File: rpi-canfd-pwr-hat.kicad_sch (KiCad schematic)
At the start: 34 parts, among them J1 Raspberry_Pi, J5 Conn_01x04_Pin, U1 CAT24C256, U2 LM73100, U5 TPS56637

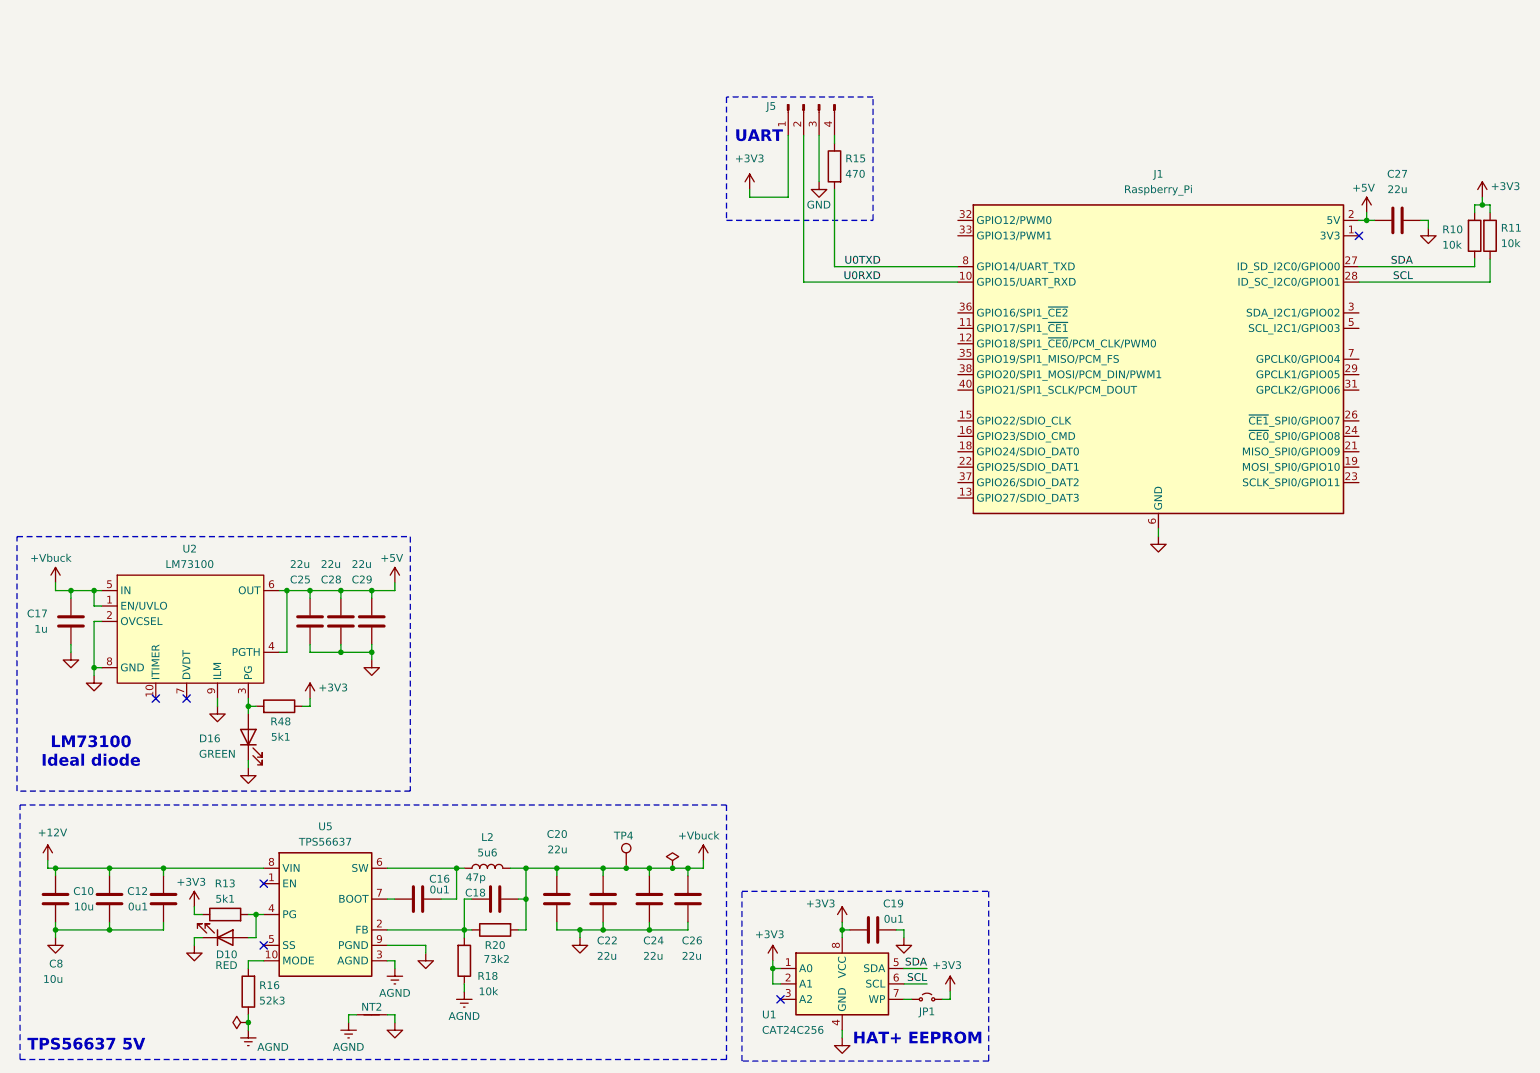
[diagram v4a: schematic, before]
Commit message: schem: add TPS259472A 5A efuse
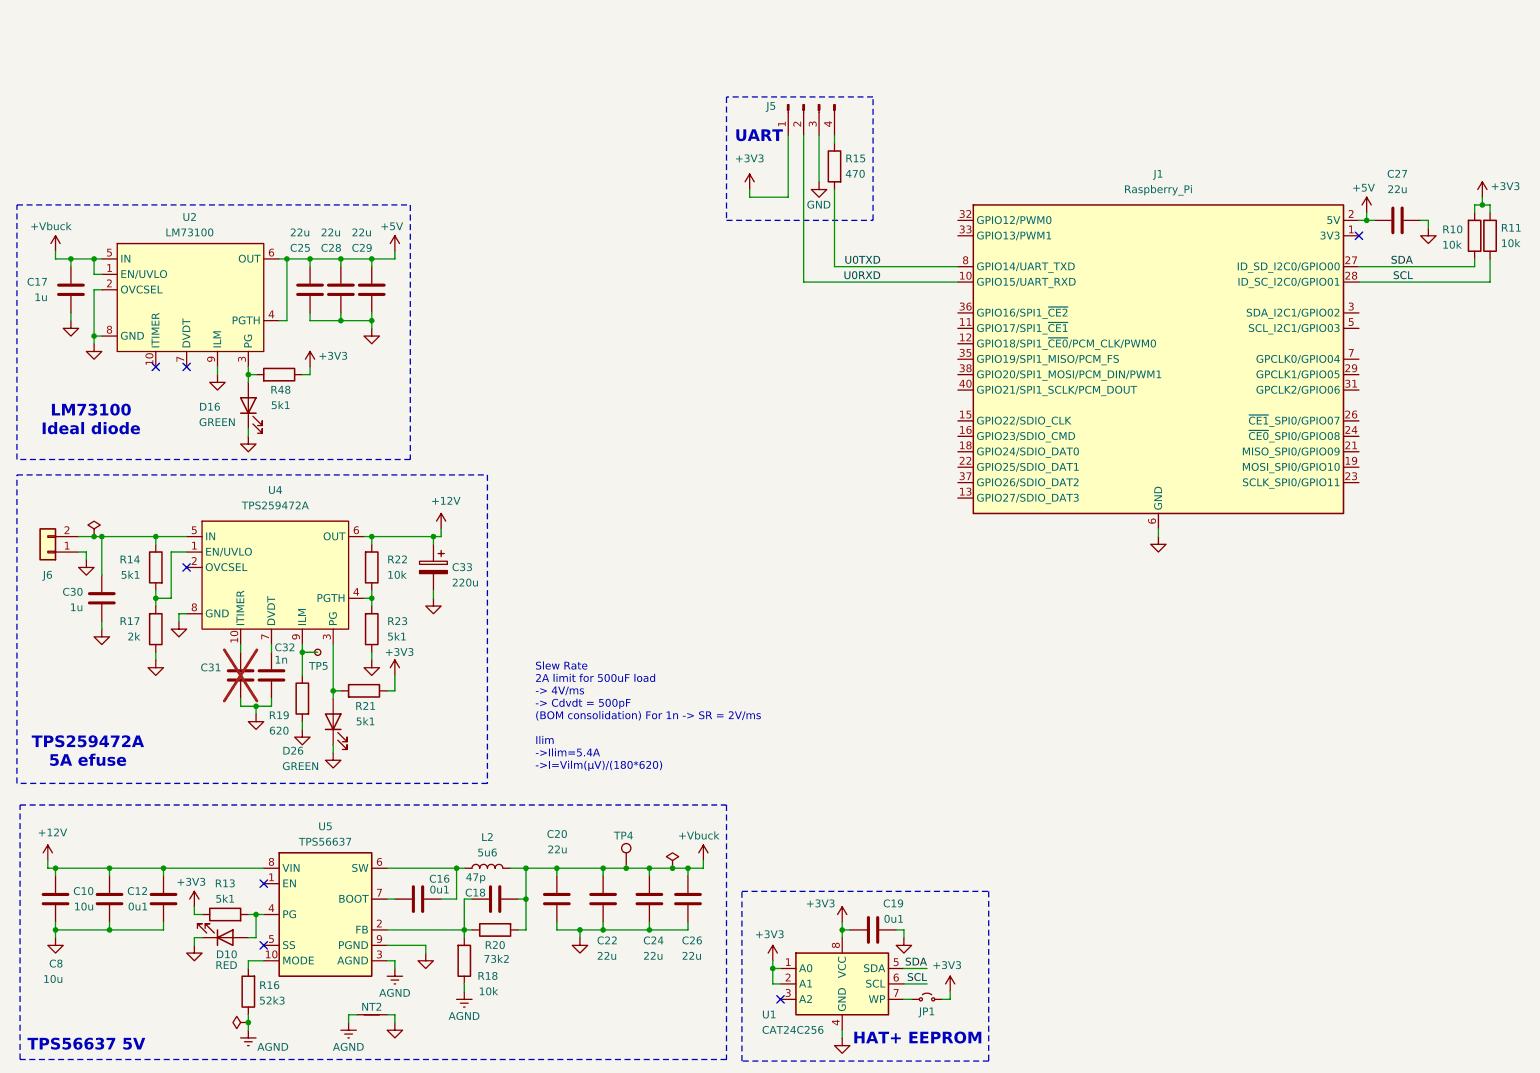
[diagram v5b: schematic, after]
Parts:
- added C30: 1u, Capacitor_SMD:C_0402_1005Metric, symbol Device:C
- added C31: C, Capacitor_SMD:C_0402_1005Metric, symbol Device:C
- added C32: 1n, Capacitor_SMD:C_0402_1005Metric, symbol Device:C
- added C33: 220u, Capacitor_SMD:CP_Elec_6.3x7.7, symbol Device:C_Polarized
- added D26: GREEN, LED_SMD:LED_0805_2012Metric, symbol Device:LED
- added J6: Conn_01x02, Connector_JST:JST_XH_B2B-XH-A_1x02_P2.50mm_Vertical, symbol Connector_Generic:Conn_01x02
- added R14, R21, R23: 5k1, Resistor_SMD:R_0402_1005Metric, symbol Device:R
- added R17: 2k, Resistor_SMD:R_0402_1005Metric, symbol Device:R
- added R19: 620, Resistor_SMD:R_0402_1005Metric, symbol Device:R
- added R22: 10k, Resistor_SMD:R_0402_1005Metric, symbol Device:R
- added TP5: TestPoint_Small, TestPoint:TestPoint_Pad_D2.0mm, symbol Connector:TestPoint_Small
- added U4: TPS259472A, GLCS:Texas_RPW0010A_VQFN-HR-10_2x2mm_P0.5mm, symbol GLCS:TPS259472x
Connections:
- net +12V: now also C33.1, R22.2, U4.6 (OUT)
- net +3V3: now also R21.1
- net GND: now also C30.1, C31.2, C32.2, C33.2, D26.1 (K), J6.1 (Pin_1), R17.1, R19.2, R23.1, U4.8 (GND)
- new net: R14.2, R17.2, U4.1 (EN/UVLO)
- new net: C31.1, U4.10 (ITIMER)
- new net: D26.2 (A), R21.2, U4.3 (PG)
- new net: R22.1, R23.2, U4.4 (PGTH)
- new net: C30.2, J6.2 (Pin_2), R14.1, U4.5 (IN)
- new net: C32.1, U4.7 (DVDT)
- new net: R19.1, TP5.1, U4.9 (ILM)
- no-connect marks 6 -> 7
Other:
- note added: "Slew Rate 2A limit for 500uF load -> 4V/ms -> Cdvdt = 500pF (BOM consolidation) For 1n -> SR = 2V/ms Ilim ->Ilim=5.4A ->I=Vilm(µV)/(180*620)"
- note added: "TPS259472A 5A efuse"
- moved on the sheet: C17, C25, C28, C29, D16, R48, U2

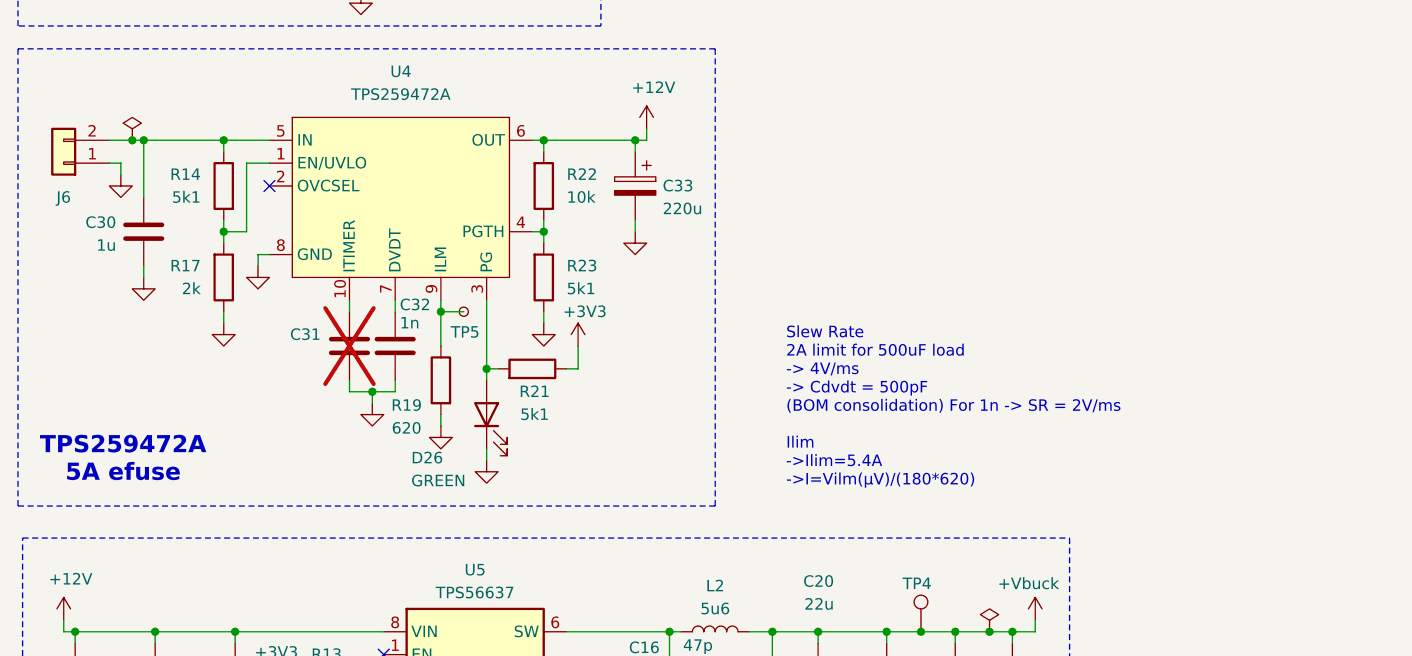
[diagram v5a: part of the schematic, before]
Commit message: schem: fix ufuse uvlo and pgth
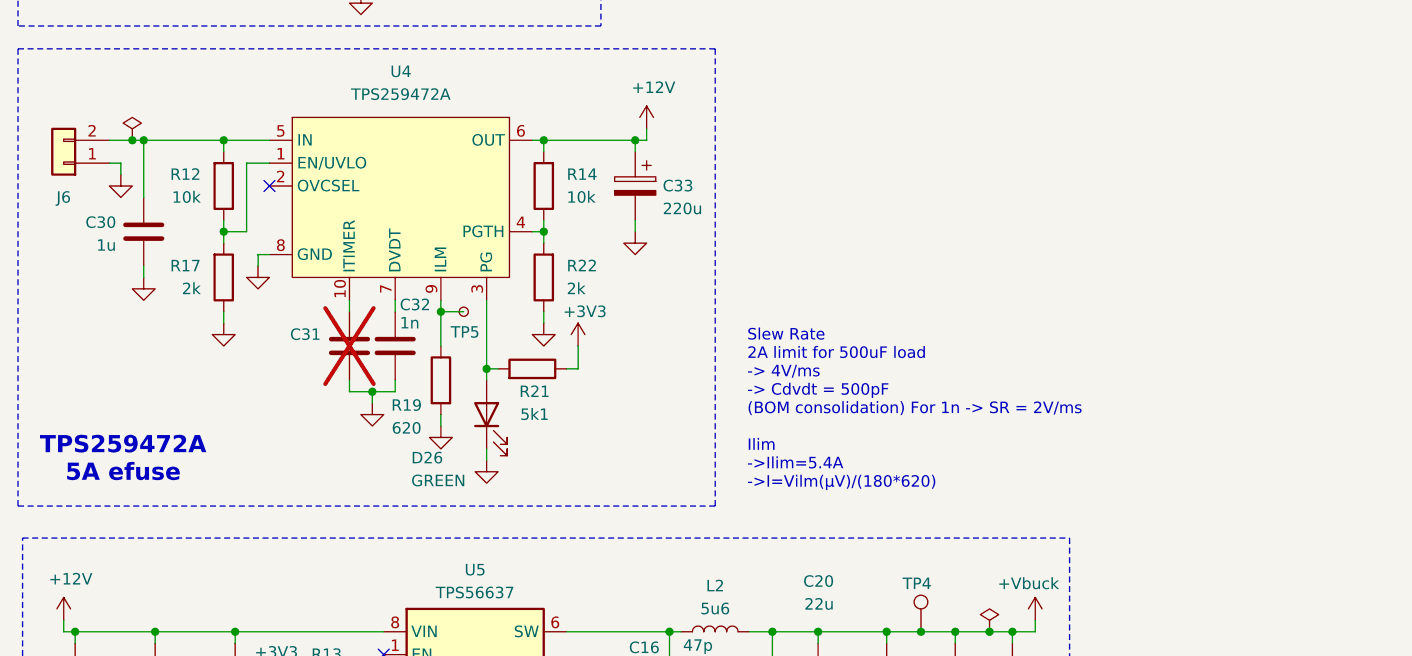
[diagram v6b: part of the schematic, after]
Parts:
- removed R23: 5k1, Resistor_SMD:R_0402_1005Metric, symbol Device:R
- added R12: 10k, Resistor_SMD:R_0402_1005Metric, symbol Device:R
- R14: value 5k1 -> 10k; JLCPCB Part # C25905 -> C25744; Manufacturer Part Number 0402WGF5101TCE -> 0402WGF1002TCE
- R22: value 10k -> 2k; JLCPCB Part # C25744 -> C4109; Manufacturer Part Number 0402WGF1002TCE -> 0402WGF2001TCE
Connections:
- net +12V: now also R14.2; no longer R22.2
- net GND: now also R22.1
- net at R17.2, U4.1 (EN/UVLO): now also R12.1; no longer R14.2
- net at U4.4 (PGTH): now also R14.1, R22.2; no longer R22.1
- net at C30.2, J6.2 (Pin_2), U4.5 (IN): now also R12.2; no longer R14.1

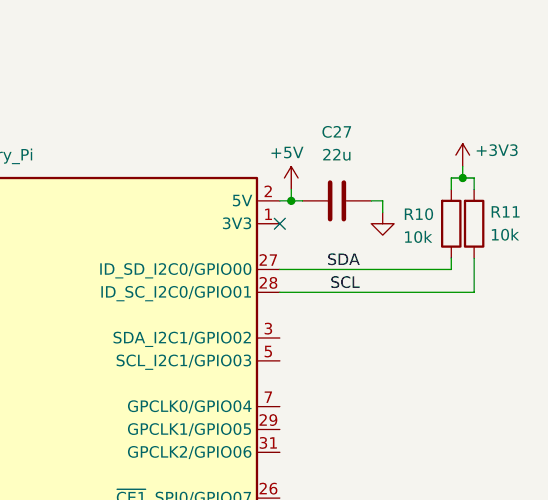
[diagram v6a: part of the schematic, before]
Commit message: schem: remove i2c pullups
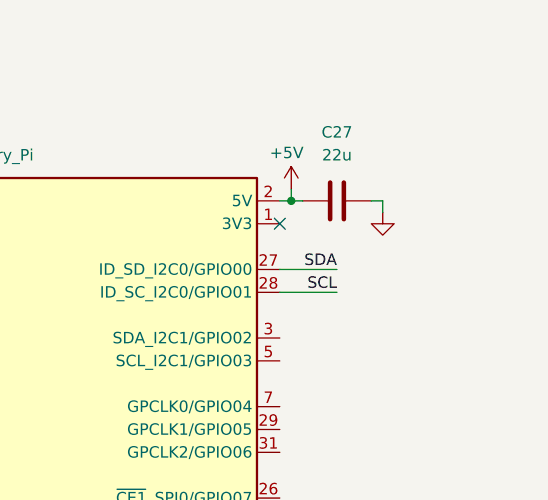
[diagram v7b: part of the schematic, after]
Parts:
- removed R10, R11: 10k, Resistor_SMD:R_0402_1005Metric, symbol Device:R

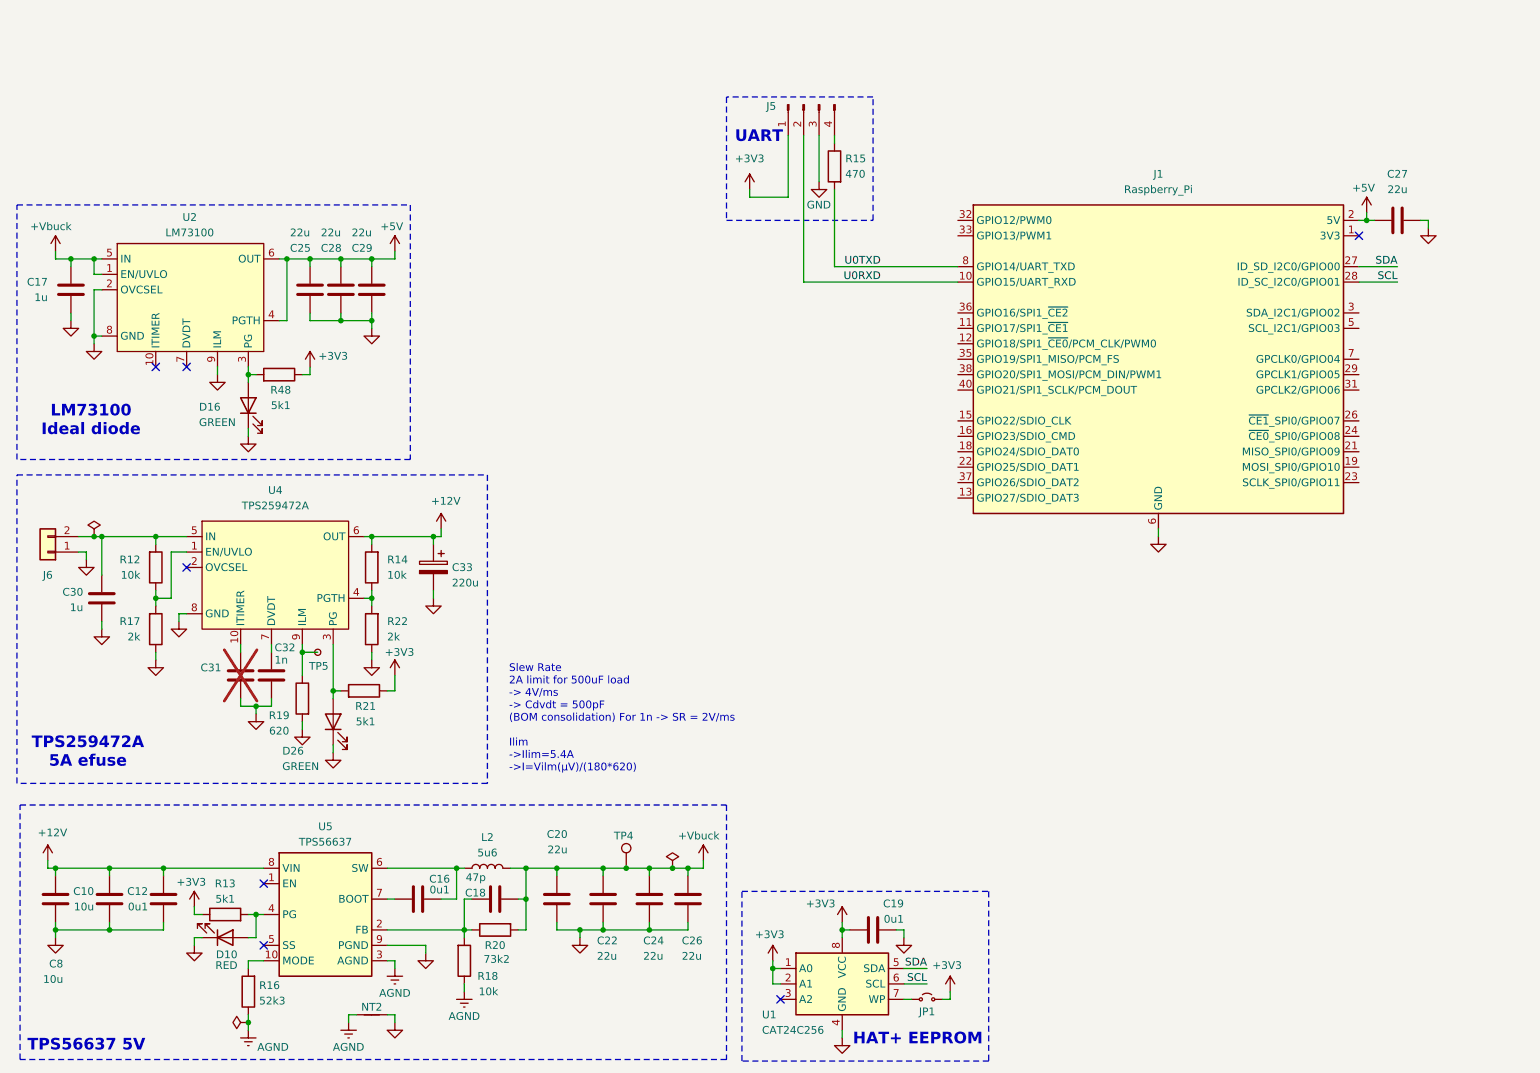
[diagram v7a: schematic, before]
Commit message: schem: add MCP2518FD CAN FD Controller
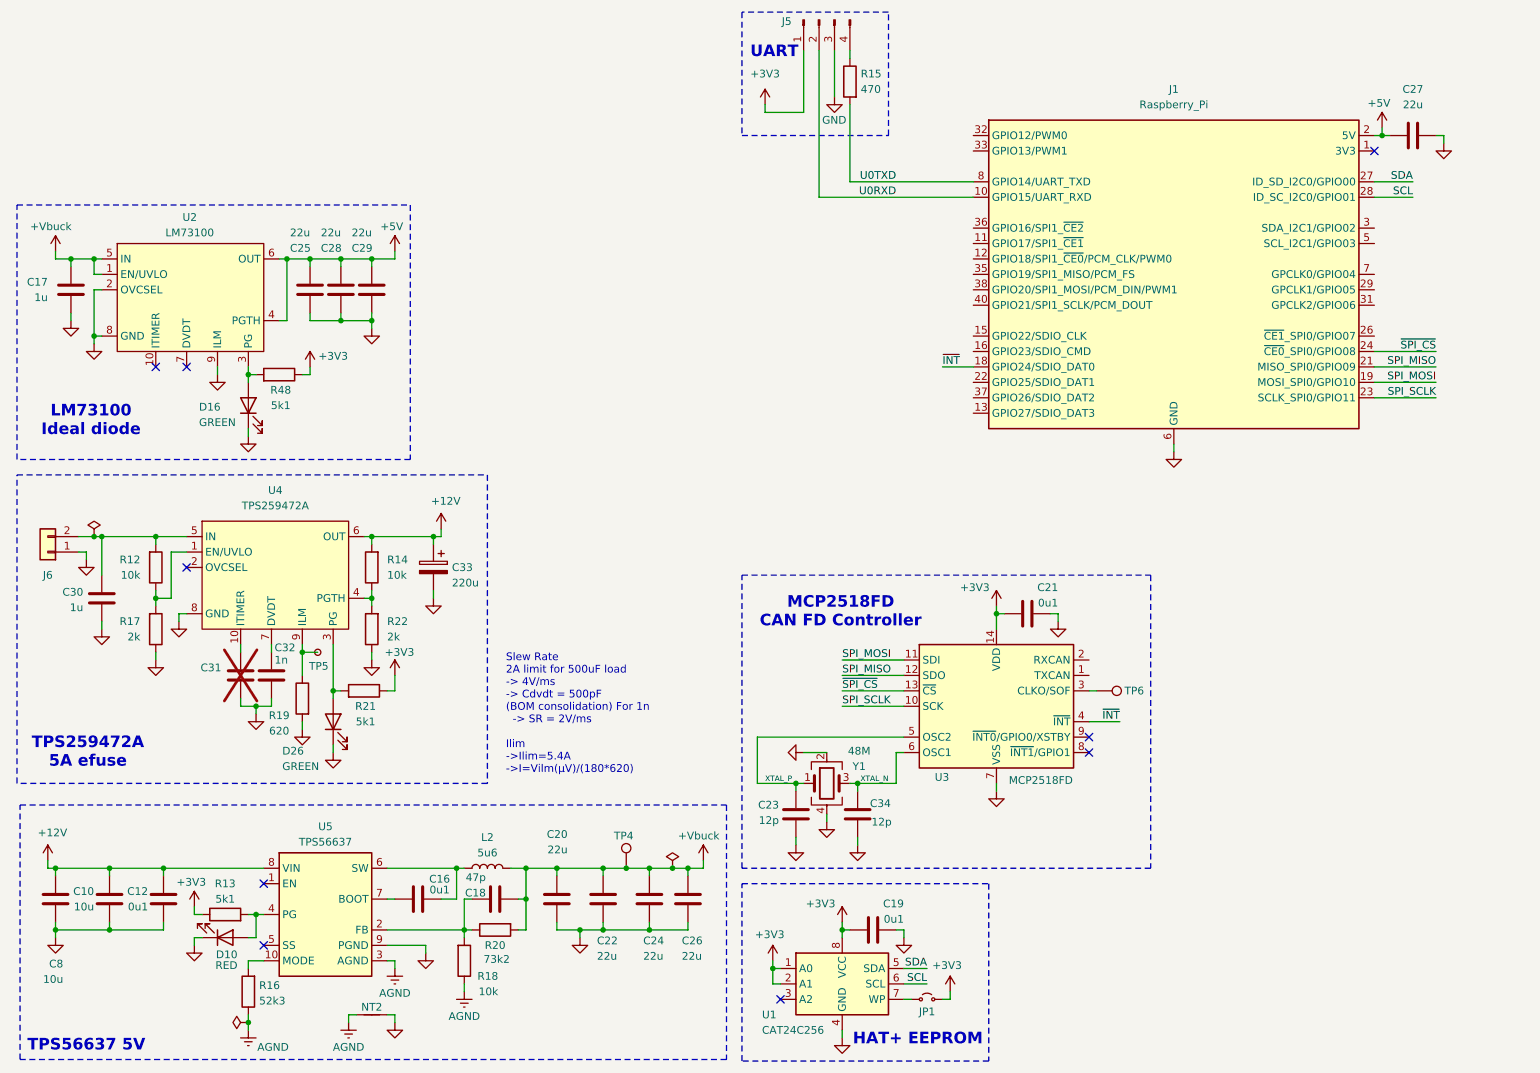
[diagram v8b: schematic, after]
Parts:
- added C21: 0u1, Capacitor_SMD:C_0402_1005Metric, symbol Device:C
- added C23, C34: 12p, Capacitor_SMD:C_0402_1005Metric, symbol Device:C
- added TP6: TestPoint, TestPoint:TestPoint_Pad_D2.0mm, symbol Connector:TestPoint
- added U3: MCP2518FD, Package_DFN_QFN:DFN-14-1EP_3x4.5mm_P0.65mm_EP1.65x4.25mm, symbol Interface_CAN_LIN:MCP2518FD-xQBB
- added Y1: 48M, Crystal:Crystal_SMD_2016-4Pin_2.0x1.6mm, symbol Device:Crystal_GND24
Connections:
- net +3V3: now also C21.1, U3.14 (VDD)
- net GND: now also C21.2, C23.1, C34.2, U3.15 (VSS), U3.7 (VSS), Y1.2, Y1.4
- net ~{INT}: now reaches J1.18 (GPIO24/SDIO_DAT0)
- net ~{INT}: now also U3.4 (~{INT})
- net SPI_MOSI: now reaches J1.19 (MOSI_SPI0/GPIO10)
- net SPI_MOSI: now also U3.11 (SDI)
- net SPI_MISO: now reaches J1.21 (MISO_SPI0/GPIO09)
- net SPI_MISO: now also U3.12 (SDO)
- net SPI_SCLK: now reaches J1.23 (SCLK_SPI0/GPIO11)
- net SPI_SCLK: now also U3.10 (SCK)
- net ~{SPI_CS}: now reaches J1.24 (~{CE0}_SPI0/GPIO08)
- net ~{SPI_CS}: now also U3.13 (~{CS})
- new net: TP6.1, U3.3 (CLKO/SOF)
- new net XTAL_N: C34.1, U3.6 (OSC1), Y1.3
- new net XTAL_P: C23.2, U3.5 (OSC2), Y1.1
- no-connect marks 7 -> 9
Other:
- note added: "MCP2518FD CAN FD Controller"
- moved on the sheet: C27, J1, J5, R15
